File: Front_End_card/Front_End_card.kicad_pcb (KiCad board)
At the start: 2 copper layers, 5 parts, among them J1 CONN_01X03, J2 CONN_01X03, J3 CONN_01X02, U1 ACS758xCB-PFF

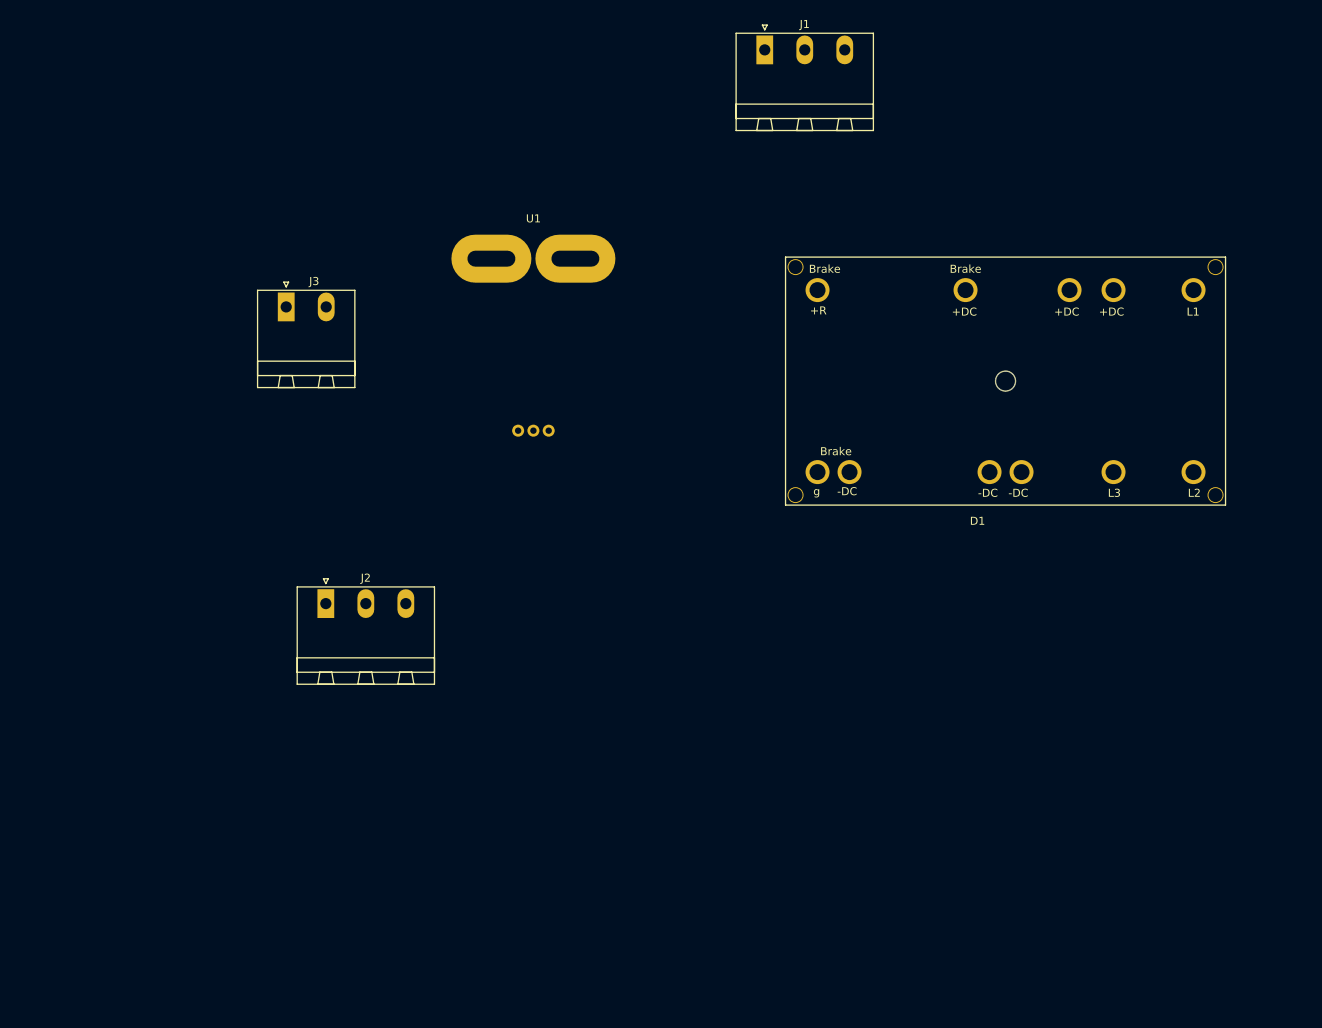
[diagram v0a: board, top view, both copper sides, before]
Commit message: Made new schematic, started PCB layout
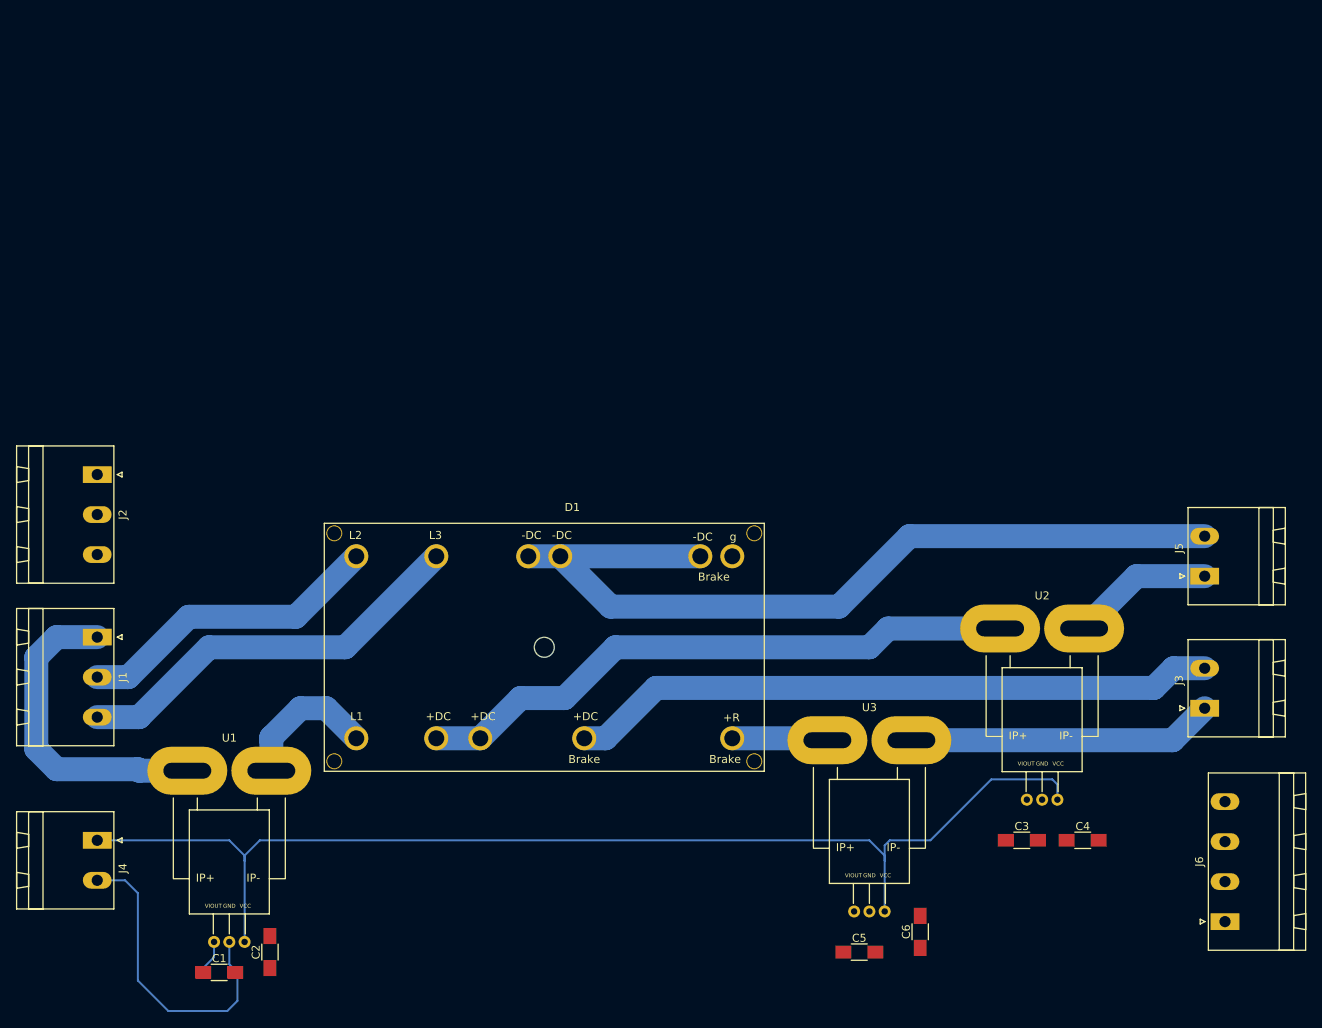
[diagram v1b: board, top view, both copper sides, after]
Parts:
- added C1: 0.1uF, Capacitors_SMD:C_1206_HandSoldering, F.Cu at (109.2, 172.7)
- added C2: C, Capacitors_SMD:C_1206_HandSoldering, F.Cu at (115.6, 170.2)
- added C3: 0.1uF, Capacitors_SMD:C_1206_HandSoldering, F.Cu at (209.6, 156.2)
- added C4: C, Capacitors_SMD:C_1206_HandSoldering, F.Cu at (217.2, 156.2)
- added C5: 0.1uF, Capacitors_SMD:C_1206_HandSoldering, F.Cu at (189.2, 170.2)
- added C6: C, Capacitors_SMD:C_1206_HandSoldering, F.Cu at (196.8, 167.6)
- added J4: CONN_01X02, Phoenix_Contact:MSTBA_25_2p_G_508-1757242, F.Cu at (94.0, 156.2)
- added J5: CONN_01X02, Phoenix_Contact:MSTBA_25_2p_G_508-1757242, F.Cu at (232.4, 123.2)
- added J6: CONN_01X04, Phoenix_Contact:MSTBA_25_4p_G_508-1757268, F.Cu at (234.9, 166.4)
- added U2: ACS758xCB-PFF, Allegro:ACS758LCB-050B-PFF-T, F.Cu at (212.1, 151.1)
- added U3: ACS758xCB-PFF, Allegro:ACS758LCB-050B-PFF-T, F.Cu at (190.5, 165.1)
- D1: footprint semikron:SK_95_DGL_126 -> Semikron:SK_95_DGL_126
- J1, J2: footprint PhoenixContact:MSTBA_25_3p_G_508-1757488 -> Phoenix_Contact:MSTBA_25_3p_G_508-1757488
- J3: footprint PhoenixContact:MSTBA_25_2p_G_508-1757242 -> Phoenix_Contact:MSTBA_25_2p_G_508-1757242
- moved J3 125.3 mm to (232.4, 139.7), turned to 90 degrees
- moved J1 111.1 mm to (94.0, 130.8), turned to 270 degrees
- moved U1 74.4 mm to (110.5, 168.9)
- moved D1 66.6 mm to (149.9, 132.1), turned to 180 degrees
- moved J2 32.8 mm to (94.0, 110.5), turned to 270 degrees
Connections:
- J1 pad 1: Net-(D1-Pad1) -> Net-(J1-Pad1)
- J3 pad 1: Net-(D1-Pad9) -> Net-(J3-Pad1)
- J3 pad 2: Net-(D1-Pad14) -> Net-(D1-Pad9)
- U1 pad 1: (no net) -> Net-(J1-Pad1)
- U1 pad 2: (no net) -> Net-(D1-Pad1)
- U1 pad 3: (no net) -> DC_in
- U1 pad 4: (no net) -> GND
- U1 pad 5: (no net) -> +5V
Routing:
- net +5V: track 0.00 -> 148.3 mm
- net Net-(D1-Pad21): track 0.00 -> 108.3 mm
- net Net-(D1-Pad9): track 0.00 -> 81.2 mm
- net Net-(D1-Pad4): track 0.00 -> 76.2 mm
- net Net-(D1-Pad18): track 0.00 -> 50.7 mm
- net Net-(J1-Pad1): track 0.00 -> 40.1 mm
- net Net-(D1-Pad15): track 0.00 -> 38.6 mm
- net GND: track 0.00 -> 38.4 mm
- net Net-(J3-Pad1): track 0.00 -> 38.3 mm
- net Net-(D1-Pad1): track 0.00 -> 18.0 mm
- net Net-(J5-Pad1): track 0.00 -> 17.8 mm
- net Net-(D1-Pad14): track 0.00 -> 12.0 mm
- net DC_in: track 0.00 -> 4.24 mm
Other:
- net class Default: clearance 0.2 -> 1; trace_width 0.25 -> 3
- net class Signals added: clearance 0.2, trace_width 0.25, via_dia 0.6, via_drill 0.4
- rule pad_to_mask_clearance: 0.2 -> 0
- rule trace_clearance: 0.2 -> 1

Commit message: Continued work on PCB layout
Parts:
- C1, C2, C3, C4, C5, C6: moved to B.Cu
- moved U3 24.6 mm to (214.6, 169.7)
- moved C6 24.5 mm to (221.0, 171.7)
- moved C5 23.6 mm to (212.6, 173.7)
- moved U2 21.2 mm to (191.5, 156.2)
- moved C3 20.7 mm to (189.5, 161.3)
- moved C4 19.5 mm to (197.9, 158.8), turned to 90 degrees
- moved C2 1.08 mm to (116.3, 170.9)
- moved C1 0.80 mm to (108.5, 173.0)
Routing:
- net +5V: track 148.3 -> 47.1 mm
- net Net-(D1-Pad9): track 81.2 -> 0.00 mm
- net Net-(D1-Pad4): track 76.2 -> 5.50 mm
- net Net-(J3-Pad1): track 38.3 -> 0.00 mm
- net Net-(J5-Pad1): track 17.8 -> 0.00 mm
- net GND: track 38.4 -> 55.6 mm
- net Net-(D1-Pad14): track 12.0 -> 0.35 mm
- net DC_out: track 0.00 -> 6.77 mm
- net BRAKE: track 0.00 -> 4.94 mm

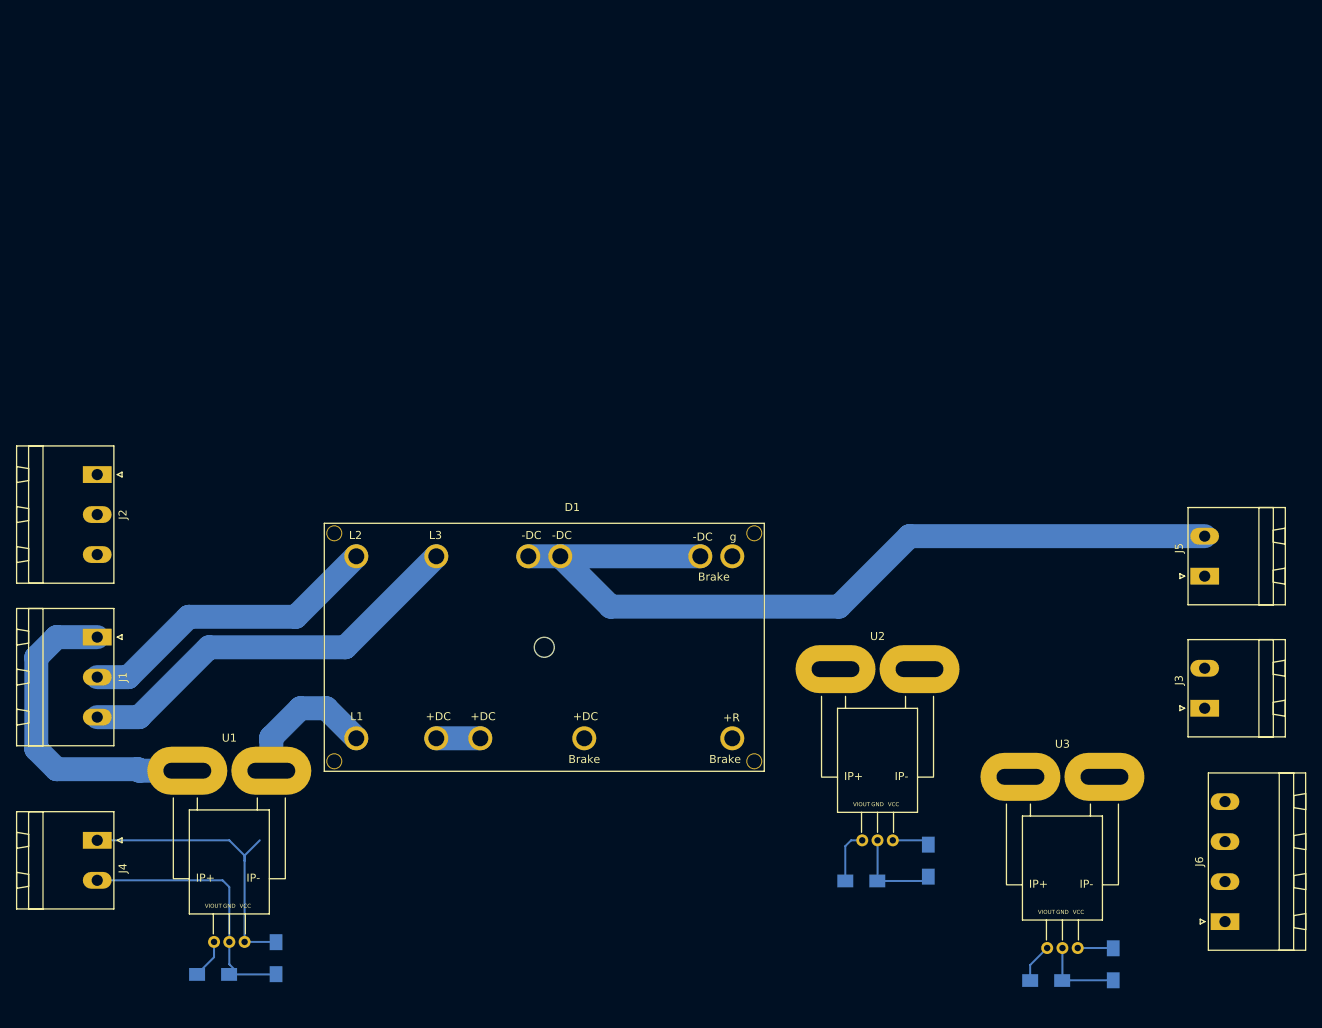
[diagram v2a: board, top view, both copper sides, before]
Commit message: Added R out current sensor output. Redesigned and finalized layout
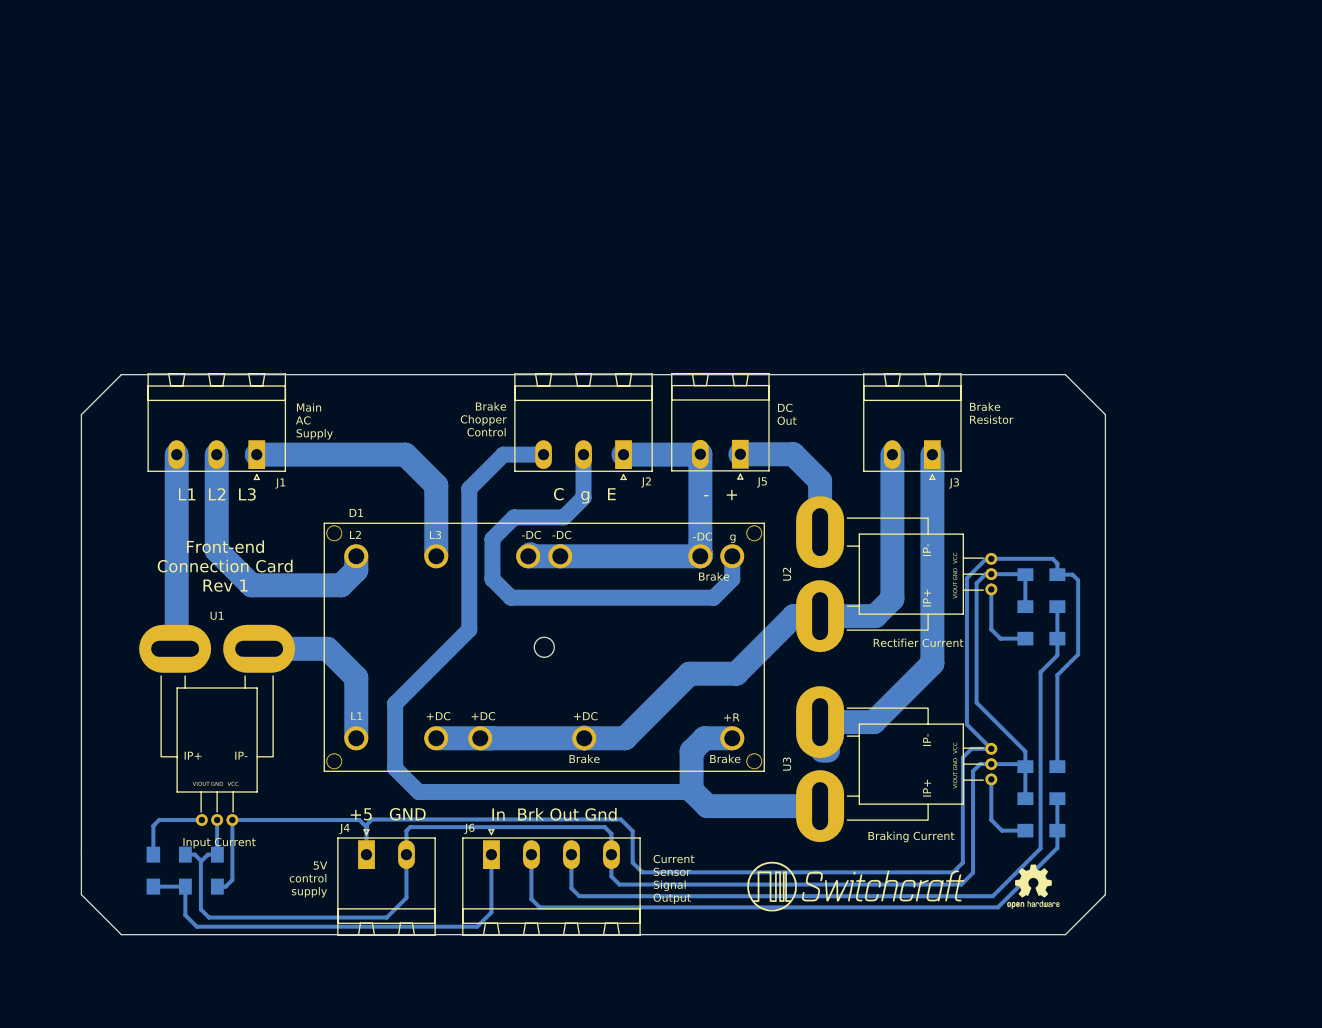
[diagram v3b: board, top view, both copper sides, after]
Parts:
- added G***: LOGO, Switchcraft:Switchcraft_medium_logo, F.Cu at (189.0, 162.0)
- added R1: R, Resistors_SMD:R_1206_HandSoldering, B.Cu at (101.0, 160.0)
- added R2: R, Resistors_SMD:R_1206_HandSoldering, B.Cu at (212.0, 131.0)
- added R3: R, Resistors_SMD:R_1206_HandSoldering, B.Cu at (212.0, 155.0)
- added REF***: OSHW-Logo2_7.3x6mm_SilkScreen, OSHW:OSHW-Logo2_7.3x6mm_SilkScreen, F.Cu at (211.0, 162.0)
- moved J6 92.1 mm to (143.3, 158.0), turned to 0 degrees
- moved J2 65.8 mm to (159.8, 108.0), turned to 180 degrees
- moved J5 60.0 mm to (174.4, 108.0), turned to 180 degrees
- moved J3 46.5 mm to (198.4, 108.0), turned to 180 degrees
- moved C3 41.0 mm to (212.0, 127.0), turned to 180 degrees
- moved C4 38.4 mm to (212.0, 123.0), turned to 0 degrees
- moved U2 36.2 mm to (205.7, 122.9), turned to 90 degrees
- moved J4 33.7 mm to (127.6, 158.0), turned to 0 degrees
- moved J1 30.3 mm to (113.9, 108.0), turned to 180 degrees
- moved C6 26.3 mm to (212.0, 147.0), turned to 0 degrees
- moved U3 24.6 mm to (205.7, 146.7), turned to 90 degrees
- moved C5 22.7 mm to (212.0, 151.0), turned to 180 degrees
- moved U1 15.3 mm to (109.0, 153.7)
- moved C1 13.4 mm to (105.0, 160.0), turned to 90 degrees
- moved C2 13.2 mm to (109.0, 160.0), turned to 270 degrees
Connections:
- D1 pad 9: Net-(D1-Pad9) -> Net-(D1-Pad4)
- J1 pad 1: Net-(J1-Pad1) -> Net-(D1-Pad18)
- J1 pad 3: Net-(D1-Pad18) -> Net-(J1-Pad3)
- J2 pad 1: Net-(D1-Pad14) -> Net-(D1-Pad21)
- J2 pad 3: Net-(D1-Pad21) -> Net-(D1-Pad14)
- J3 pad 2: Net-(D1-Pad9) -> Net-(D1-Pad4)
- J6 pad 2: DC_out -> BRAKE
- J6 pad 3: BRAKE -> DC_out
- U1 pad 1: Net-(J1-Pad1) -> Net-(J1-Pad3)
- U1 pad 3: DC_in -> Net-(R1-Pad2)
- U2 pad 3: DC_out -> Net-(R2-Pad2)
- U3 pad 3: BRAKE -> Net-(R3-Pad2)
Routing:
- net +5V: track 47.1 -> 191.9 mm
- net GND: track 55.6 -> 189.5 mm
- net Net-(D1-Pad14): track 0.35 -> 115.8 mm
- net DC_out: track 6.77 -> 96.8 mm
- net Net-(D1-Pad4): track 5.50 -> 83.8 mm
- net BRAKE: track 4.94 -> 81.0 mm
- net Net-(D1-Pad21): track 108.3 -> 44.4 mm
- net Net-(D1-Pad28): track 0.00 -> 58.7 mm
- net DC_in: track 4.24 -> 54.4 mm
- net Net-(J3-Pad1): track 0.00 -> 43.9 mm
- net Net-(J1-Pad1): track 40.1 -> 0.00 mm
- net Net-(J1-Pad3): track 0.00 -> 24.3 mm
- net Net-(D1-Pad18): track 50.7 -> 32.9 mm
- net Net-(J5-Pad1): track 0.00 -> 17.7 mm
- net Net-(R3-Pad2): track 0.00 -> 9.98 mm
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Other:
- board outline added: 128 x 70 mm
- net class Default: trace_width 3 -> 2
- net class Signals: trace_width 0.25 -> 0.5
- board text added: "+5 GND"
- board text added: "- +"
- board text added: "5V control supply"
- board text added: "Brake Chopper Control"
- board text added: "Brake Resistor"
- board text added: "Braking Current"
- board text added: "C g E"
- board text added: "Current Sensor Signal Output"
- board text added: "DC Out"
- board text added: "Front-end Connection Card Rev 1"
- board text added: "I have a million ideas. They all point to certain death."
- board text added: "In Brk Out Gnd"
- board text added: "Input Current"
- board text added: "L1 L2 L3"
- board text added: "Main AC Supply"
- board text added: "Rectifier Current"
- board text added: "Yngve was here"
